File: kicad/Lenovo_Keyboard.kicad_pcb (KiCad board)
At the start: 2 copper layers, 100 x 37 mm, 14 parts, among them J1 Conn_01x34_Pin, J2 Conn_01x04_Socket, J3 Conn_01x04_Socket

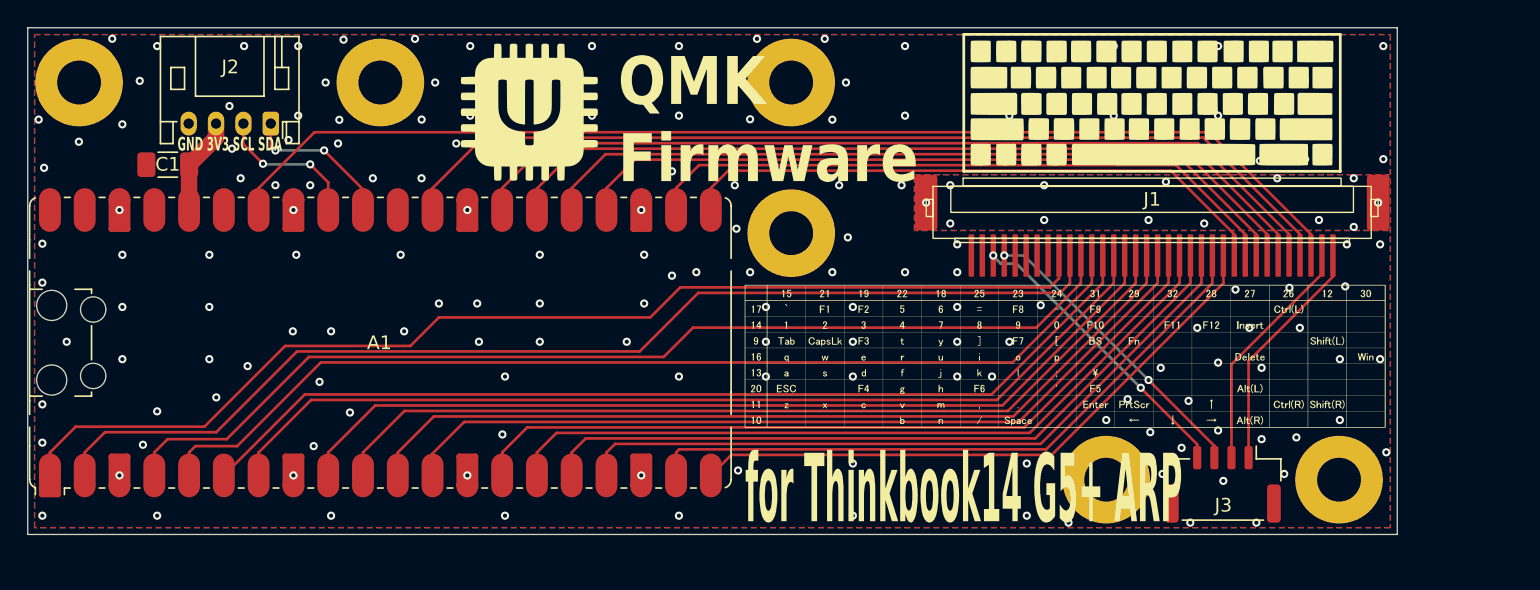
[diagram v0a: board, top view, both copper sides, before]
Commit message: SOIC-16 version
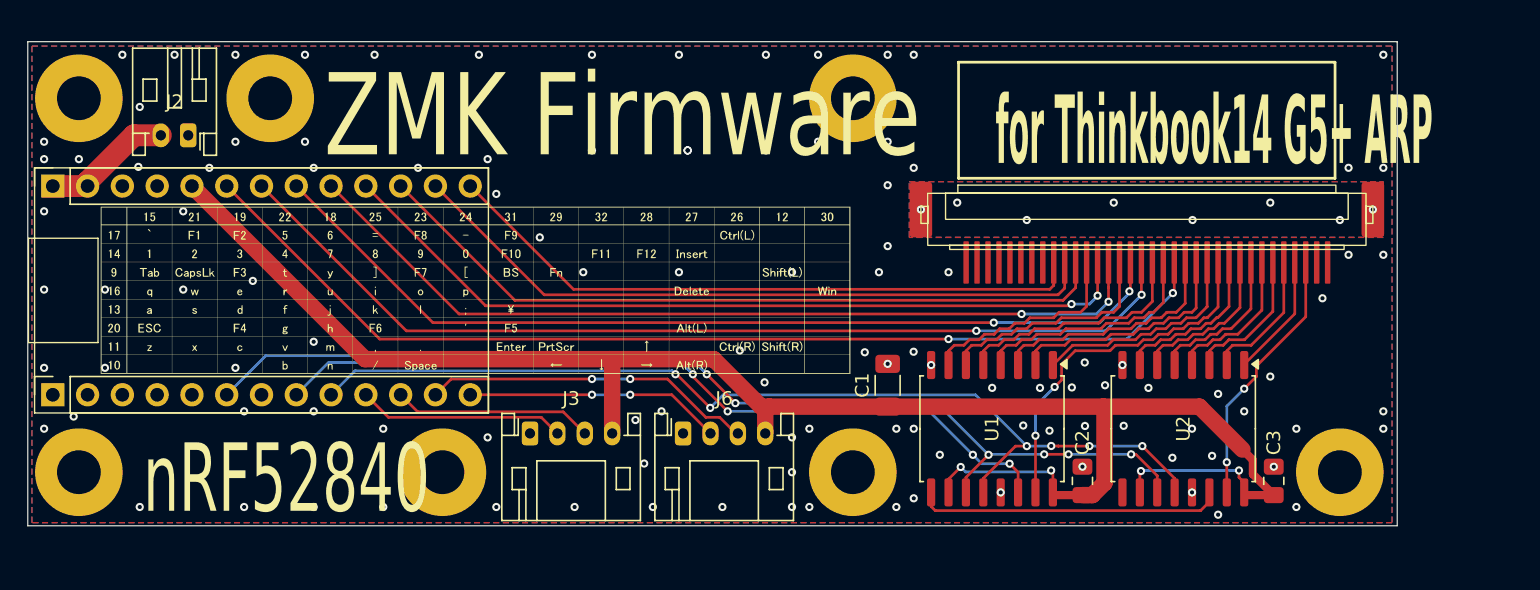
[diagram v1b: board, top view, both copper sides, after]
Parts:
- removed A1: RaspberryPi_Pico, Module:RaspberryPi_Pico_Common_SMD
- removed the G*** at (212.3, 57.5)
- removed the G*** at (166.9, 58.2)
- removed the G*** at (206.0, 75.9)
- removed the REF** at (209.0, 85.0)
- removed the REF** at (186.0, 67.0)
- removed the REF** at (186.0, 56.0)
- removed the REF** at (134.0, 56.0)
- removed the REF** at (156.0, 56.0)
- removed the REF** at (226.0, 85.0)
- added C2: 0.1uF, Capacitor_SMD:C_0805_2012Metric_Pad1.18x1.45mm_HandSolder, F.Cu at (207.3, 85.1)
- added C3: 0.1uF, Capacitor_SMD:C_0805_2012Metric_Pad1.18x1.45mm_HandSolder, F.Cu at (221.2, 85.1)
- added G***: LOGO, LOGO, F.Cu at (162.9, 71.1)
- added J4: Conn_01x13_Socket, Connector_PinSocket_2.54mm:PinSocket_1x13_P2.54mm_Vertical, F.Cu at (132.1, 78.8)
- added J5: Conn_01x13_Socket, Connector_PinSocket_2.54mm:PinSocket_1x13_P2.54mm_Vertical, F.Cu at (132.1, 63.6)
- added J6: Conn_01x04_Socket, Connector_JST:JST_PH_S4B-PH-K_1x04_P2.00mm_Horizontal, F.Cu at (178.1, 81.6)
- added REF**: MountingHole_3.2mm_M3_Pad, MountingHole:MountingHole_3.2mm_M3_Pad, F.Cu at (148.0, 57.1)
- added REF**: MountingHole_3.2mm_M3_Pad, MountingHole:MountingHole_3.2mm_M3_Pad, F.Cu at (160.5, 84.5)
- added REF**: MountingHole_3.2mm_M3_Pad, MountingHole:MountingHole_3.2mm_M3_Pad, F.Cu at (190.5, 84.5)
- added REF**: MountingHole_3.2mm_M3_Pad, MountingHole:MountingHole_3.2mm_M3_Pad, F.Cu at (226.1, 84.5)
- added REF**: MountingHole_3.2mm_M3_Pad, MountingHole:MountingHole_3.2mm_M3_Pad, F.Cu at (190.5, 57.1)
- added REF**: MountingHole_3.2mm_M3_Pad, MountingHole:MountingHole_3.2mm_M3_Pad, F.Cu at (134.0, 57.1)
- added REF**: MountingHole_3.2mm_M3_Pad, MountingHole:MountingHole_3.2mm_M3_Pad, F.Cu at (134.0, 84.5)
- added U1: 74HC595, Package_SO:SOIC-16W_7.5x10.3mm_P1.27mm, F.Cu at (200.7, 81.3)
- added U2: 74HC595, Package_SO:SOIC-16W_7.5x10.3mm_P1.27mm, F.Cu at (214.6, 81.3)
- J2: value Conn_01x04_Socket -> Conn_01x02_Pin; footprint Connector_JST:JST_PH_S4B-PH-K_1x04_P2.00mm_Horizontal -> Connector_JST:JST_PH_S2B-PH-K_1x02_P2.00mm_Horizontal
- J3: footprint Connector_JST:JST_GH_BM04B-GHS-TBT_1x04-1MP_P1.25mm_Vertical -> Connector_JST:JST_PH_S4B-PH-K_1x04_P2.00mm_Horizontal
- moved C1 55.0 mm to (193.0, 78.1), turned to 90 degrees
- moved J3 50.7 mm to (166.9, 81.6), turned to 0 degrees
- moved J2 6.09 mm to (142.0, 59.9)
- moved J1 0.64 mm to (212.0, 66.0)
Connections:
- J1 pad 10: Net-(A1-GPIO1) -> row01
- J1 pad 11: Net-(A1-GPIO2) -> row02
- J1 pad 12: Net-(A1-GPIO3) -> col07
- J1 pad 13: Net-(A1-GPIO4) -> row03
- J1 pad 14: Net-(A1-GPIO5) -> row04
- J1 pad 15: Net-(A1-GPIO6) -> col06
- J1 pad 16: Net-(A1-GPIO7) -> row05
- J1 pad 17: Net-(A1-GPIO8) -> row06
- J1 pad 18: Net-(A1-GPIO9) -> col05
- J1 pad 19: Net-(A1-GPIO10) -> col04
- J1 pad 20: Net-(A1-GPIO11) -> row07
- J1 pad 21: Net-(A1-GPIO12) -> col03
- J1 pad 22: Net-(A1-GPIO13) -> col02
- J1 pad 23: Net-(A1-GPIO14) -> col01
- J1 pad 24: Net-(A1-GPIO15) -> col00
- J1 pad 25: PFC25 -> col15
- J1 pad 26: PFC26 -> col14
- J1 pad 27: PFC27 -> col13
- J1 pad 28: PFC28 -> col12
- J1 pad 29: PFC29 -> col11
- J1 pad 3: PFC_N0 -> unconnected-(J1-Pin_3-Pad3)
- J1 pad 30: PFC30 -> col10
- J1 pad 31: PFC31 -> col09
- J1 pad 32: PFC32 -> col08
- J1 pad 33: PFC_N2 -> unconnected-(J1-Pin_33-Pad33)
- J1 pad 34: PFC_N3 -> unconnected-(J1-Pin_34-Pad34)
- J1 pad 4: PFC_N1 -> unconnected-(J1-Pin_4-Pad4)
- J1 pad 9: Net-(A1-GPIO0) -> row00
- J2 pad 1: SDA -> GND
- J2 pad 2: SCL -> BAT+
- J3 pad 1: PFC_N3 -> GND
- J3 pad 2: PFC_N2 -> SDA
- J3 pad 3: PFC_N1 -> SCL
- J3 pad 4: PFC_N0 -> +3V3
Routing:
- net +3V3: track 7.13 -> 129.8 mm, vias 0 -> 4
- net PFC32: track 84.8 -> 0.00 mm
- net Net-(A1-GPIO0): track 81.8 -> 0.00 mm
- net Net-(A1-GPIO1): track 80.3 -> 0.00 mm
- net SCLK: track 0.00 -> 77.4 mm, vias 0 -> 6
- net row07: track 0.00 -> 77.4 mm, vias 0 -> 2
- net Net-(A1-GPIO2): track 76.0 -> 0.00 mm
- net Net-(A1-GPIO3): track 74.3 -> 0.00 mm
- net CS: track 0.00 -> 72.6 mm, vias 0 -> 6
- net row06: track 0.00 -> 72.1 mm, vias 0 -> 2
- net Net-(A1-GPIO4): track 71.5 -> 0.00 mm
- net PFC31: track 70.9 -> 0.00 mm
- net Net-(A1-GPIO5): track 70.8 -> 0.00 mm
- net row05: track 0.00 -> 68.1 mm, vias 0 -> 2
- net Net-(A1-GPIO6): track 66.5 -> 0.00 mm
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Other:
- board size 100 x 37 mm -> 100 x 35.3 mm
- board text added: "ZMK Firmware"
- board text added: "nRF52840"
- board text removed: "GND 3V3 SCL SDA"
- board text removed: "QMK Firmware"

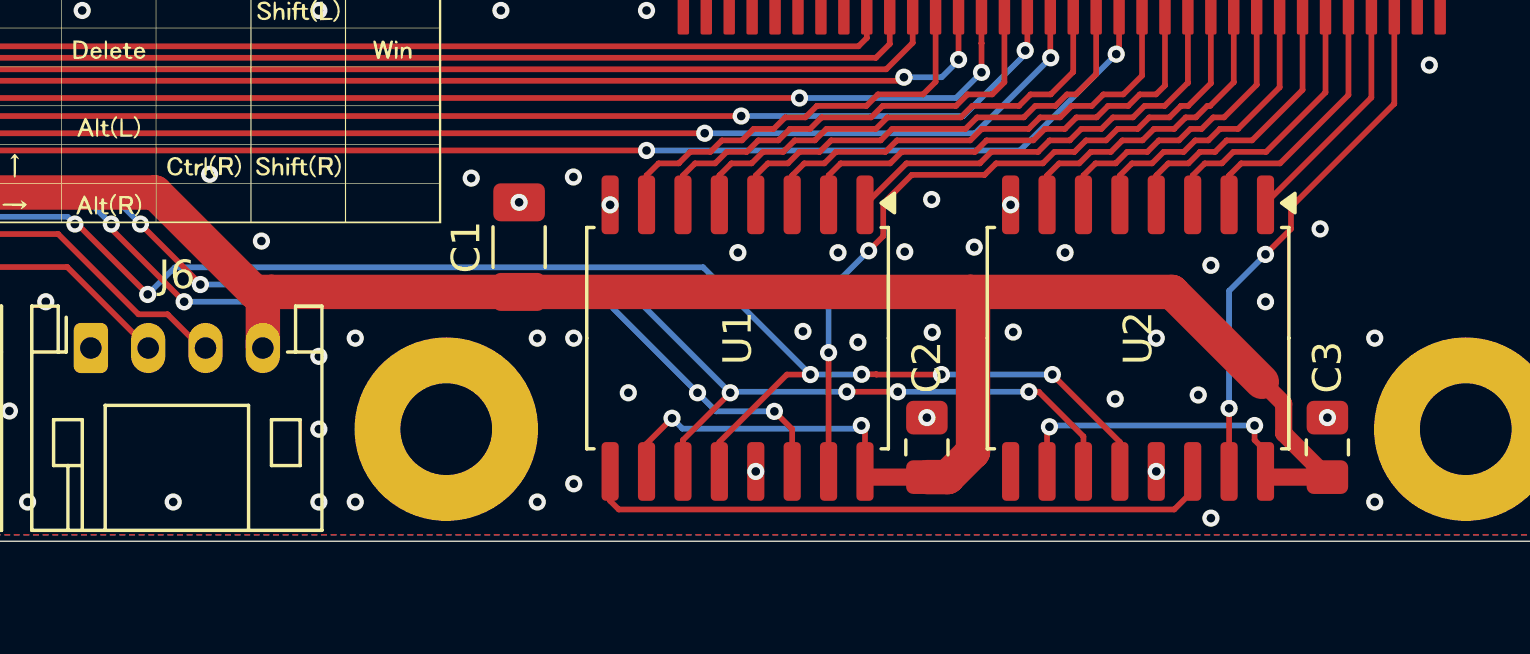
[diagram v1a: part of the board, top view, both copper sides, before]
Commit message: SOP-16 version
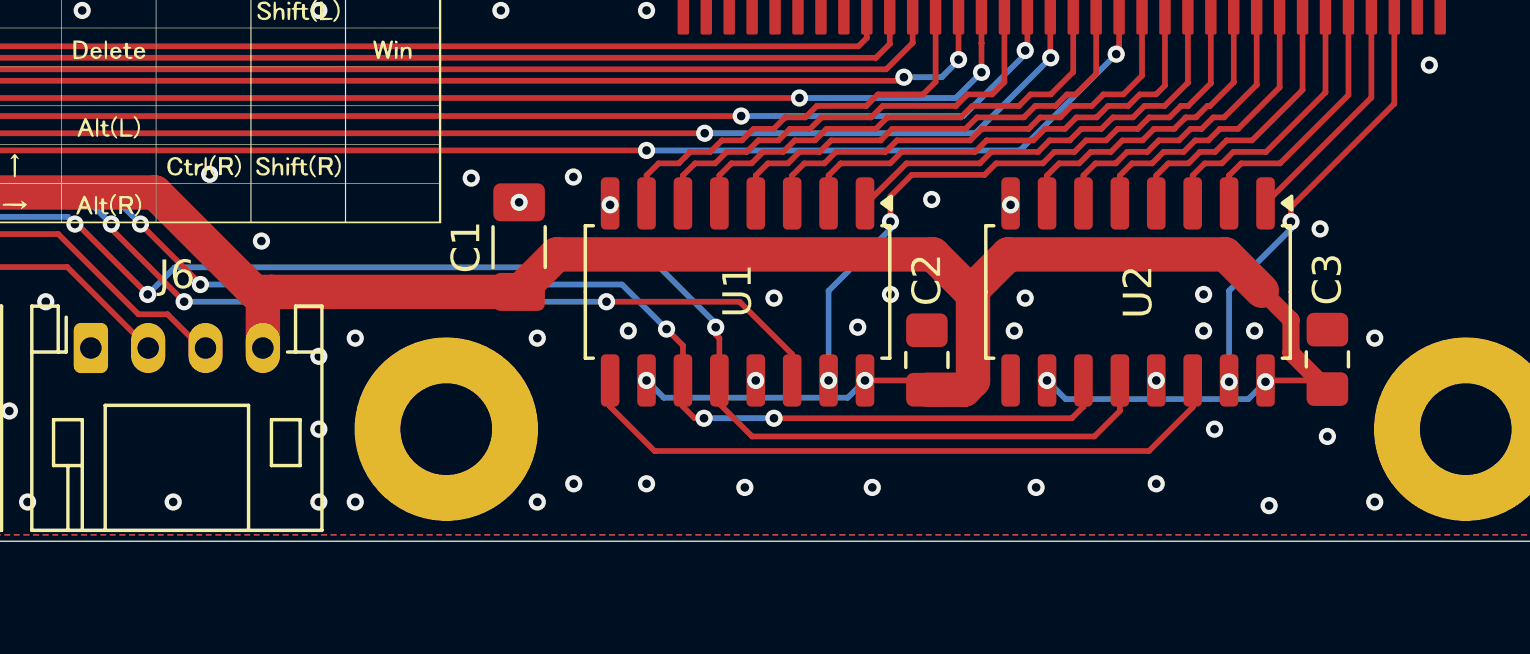
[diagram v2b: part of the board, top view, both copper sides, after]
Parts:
- U1, U2: footprint Package_SO:SOIC-16W_7.5x10.3mm_P1.27mm -> Package_SO:SOP-16_4.4x10.4mm_P1.27mm
- moved C3 3.07 mm to (221.2, 82.0)
- moved C2 3.05 mm to (207.3, 82.0)
- moved U1 1.61 mm to (200.7, 79.7)
- moved U2 1.61 mm to (214.6, 79.7)
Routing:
- net +3V3: track 129.8 -> 123.2 mm
- net CS: track 72.6 -> 69.3 mm, vias 6 -> 3
- net col00: track 26.6 -> 23.4 mm
- net col08: track 19.2 -> 16.1 mm
- net SCLK: track 77.4 -> 74.8 mm, vias 6 -> 5
- net MOSI: track 58.6 -> 56.9 mm, vias 4 -> 3
- net Net-(U1-QH'): track 22.4 -> 23.4 mm
- net GND: vias 114 -> 112

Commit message: update project
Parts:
- removed G***: LOGO, LOGO
- removed J6: Conn_01x04_Socket, Connector_JST:JST_PH_S4B-PH-K_1x04_P2.00mm_Horizontal
- J1: footprint Connector:FFC-PFC_0.8mm_34Pin -> 0000_Library:FFC-PFC_0.8mm_34Pin
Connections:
- J1 pad 3: unconnected-(J1-Pin_3-Pad3) -> GND
- J1 pad 33: unconnected-(J1-Pin_33-Pad33) -> GND
- J1 pad 34: unconnected-(J1-Pin_34-Pad34) -> LED_CAPSLK
- J1 pad 4: unconnected-(J1-Pin_4-Pad4) -> LED_ESC
- J4 pad 12: GP_0 -> LED_ESC
- J4 pad 13: GP_1 -> LED_CAPSLK
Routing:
- net LED_CAPSLK: track 0.00 -> 70.9 mm, vias 0 -> 6
- net LED_ESC: track 0.00 -> 49.1 mm, vias 0 -> 6
- net GP_0: track 24.2 -> 0.00 mm, vias 2 -> 0
- net GP_1: track 18.7 -> 0.00 mm, vias 2 -> 0
- net GND: track 0.00 -> 7.87 mm, vias 112 -> 119
- net +3V3: track 123.2 -> 121.1 mm
- net Earth: vias 8 -> 18
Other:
- board text removed: "ZMK Firmware"
